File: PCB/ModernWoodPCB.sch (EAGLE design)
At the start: 235 parts, among them Q2 FS8205, U1 ESP32-S3HOLE, U2 ME6211C33M5G

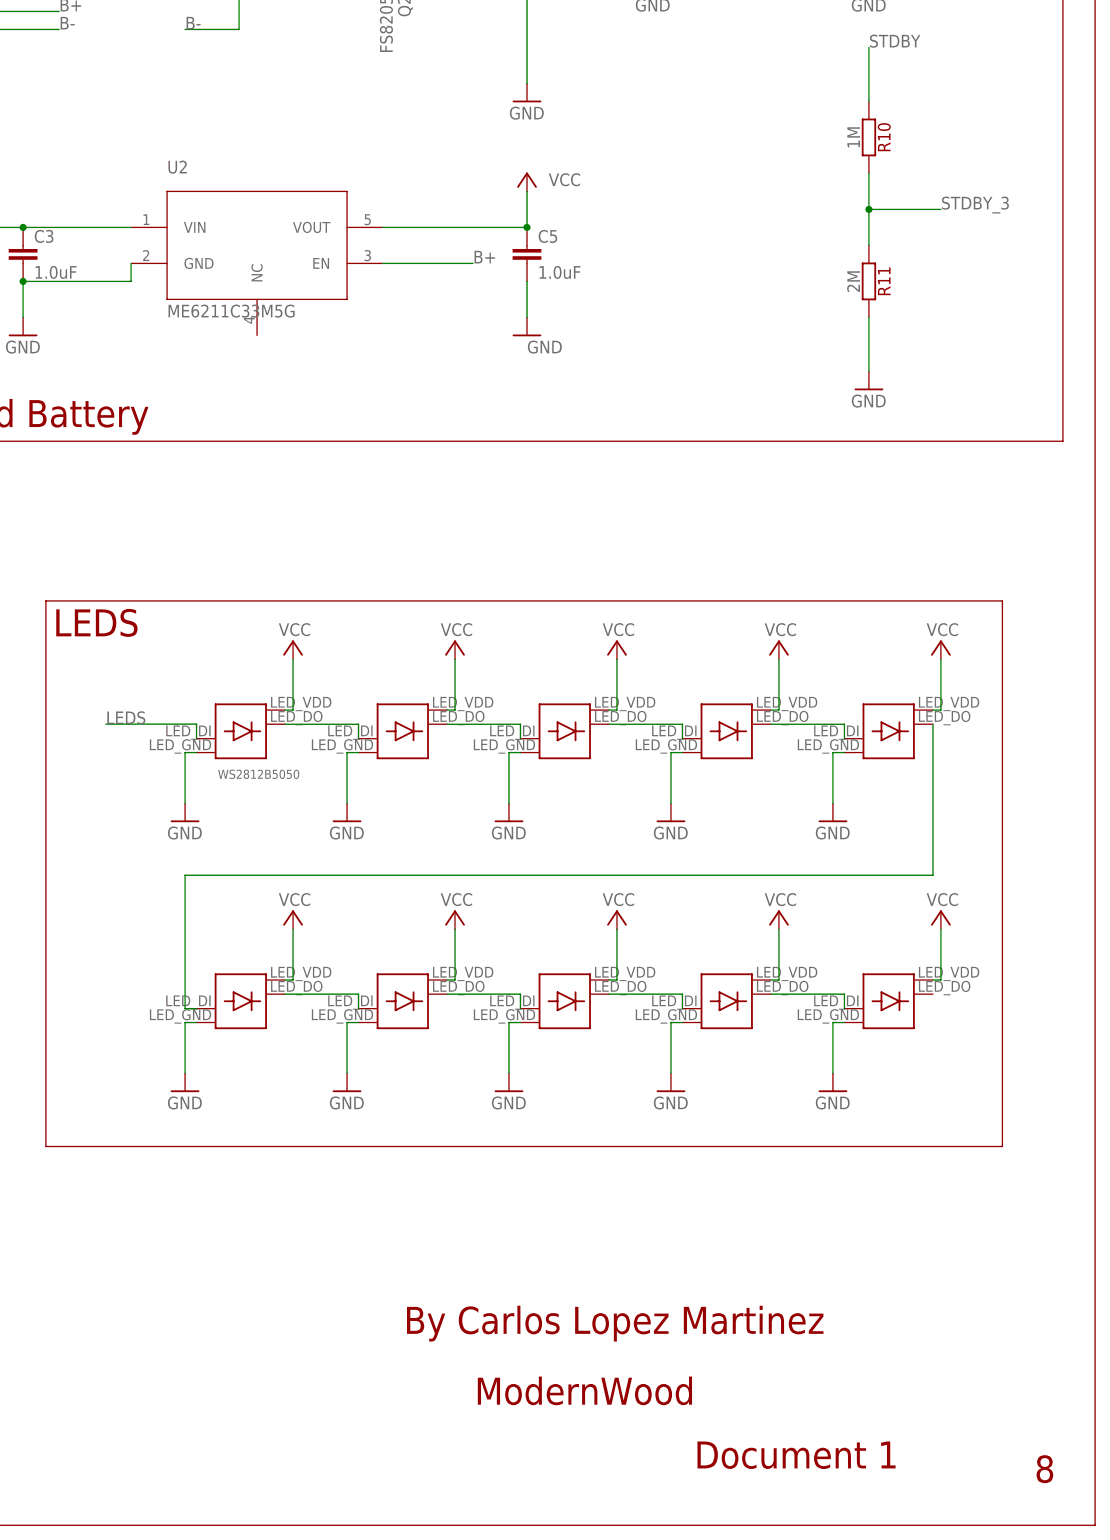
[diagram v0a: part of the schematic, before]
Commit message: New review of Schematic and added a voltage regulator diode protection
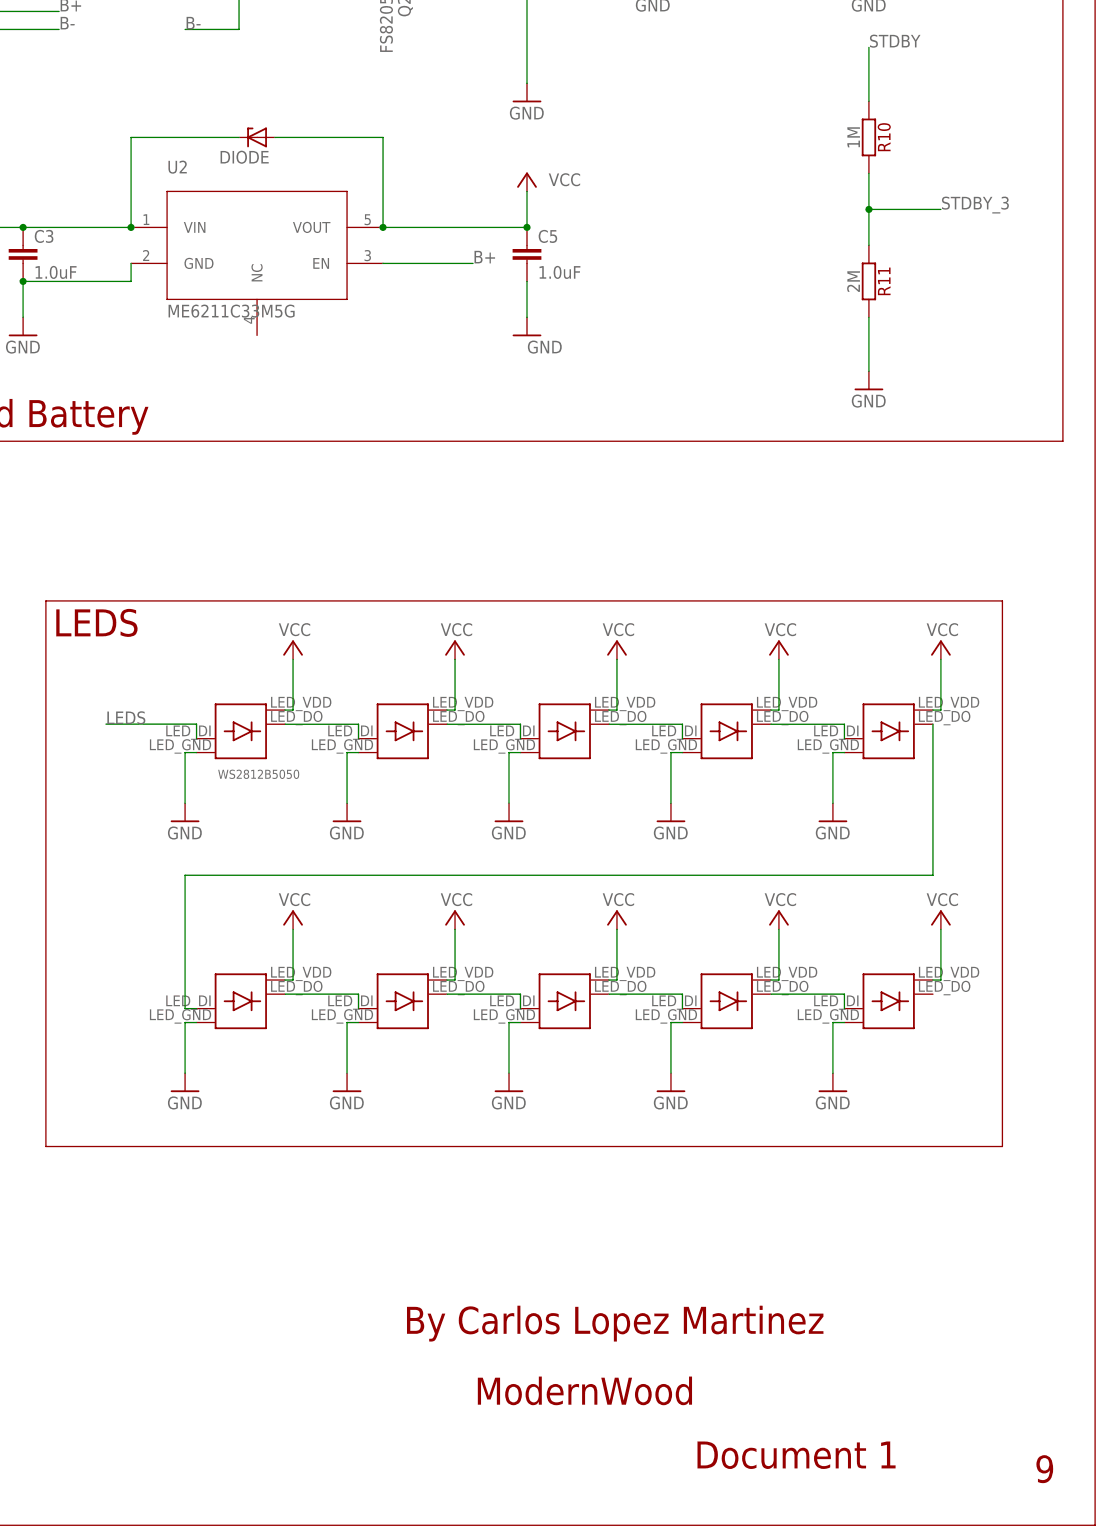
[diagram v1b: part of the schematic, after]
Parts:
- added DIODE: (no value), bt_diode:ZENER-DIODE-SOD123
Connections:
- net B+: now also DIODE.C
- net VCC: now also DIODE.A
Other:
- note added: "9"
- note removed: "8"
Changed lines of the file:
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@@
 <part name="R11" library="resistors" deviceset="?" device="1K" value="2M"/>
 <part name="GND29" library="supply1" library_urn="urn:adsk.eagle:library:371" deviceset="GND" device=""/>
+<part name="DIODE" library="bt_diode" deviceset="ZENER-DIODE" device="-SOD123"/>
 </parts>
 <sheets>
@@
 <plain>
 <text x="693.52" y="45.02" size="3.81" layer="94">ModernWood</text>
-<text x="772.52" y="34.02" size="3.81" layer="94">8</text>
+<text x="772.52" y="34.02" size="3.81" layer="94">9</text>
 <text x="724.52" y="36.02" size="3.81" layer="94">Document 1</text>
 <text x="683.52" y="55.02" size="3.81" layer="94">By Carlos Lopez Martinez</text>
@@
 <attribute name="VALUE" x="746.64" y="185.78" size="1.778" layer="96"/>
 </instance>
+<instance part="DIODE" gate="D1" x="662.82" y="223.88" smashed="yes" rot="R180">
+<attribute name="NAME" x="664.598" y="221.975" size="1.778" layer="95" rot="R180"/>
+<attribute name="VALUE" x="664.598" y="227.309" size="1.778" layer="96" rot="R180"/>
+</instance>
 </instances>
 <busses>
@@
 <junction x="700.92" y="211.18"/>
 <pinref part="P+5" gate="VCC" pin="VCC"/>
+<pinref part="DIODE" gate="D1" pin="A"/>
+<wire x1="665.36" y1="223.88" x2="680.6" y2="223.88" width="0.1524" layer="91"/>
+<wire x1="680.6" y1="223.88" x2="680.6" y2="211.18" width="0.1524" layer="91"/>
+<junction x="680.6" y="211.18"/>
 </segment>
 <segment>
@@
 <junction x="629.8" y="211.18"/>
 <label x="617.1" y="211.18" size="1.778" layer="95"/>
+<pinref part="DIODE" gate="D1" pin="C"/>
+<wire x1="645.04" y1="211.18" x2="645.04" y2="223.88" width="0.1524" layer="91"/>
+<wire x1="645.04" y1="223.88" x2="660.28" y2="223.88" width="0.1524" layer="91"/>
+<junction x="645.04" y="211.18"/>
 </segment>
 <segment>
